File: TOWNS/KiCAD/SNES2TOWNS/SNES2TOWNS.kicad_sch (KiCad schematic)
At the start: 13 parts, among them J1 DE9_Receptacle, J2 ArduinoP2_P7, J3 ArduinoP8_P13, J4 ArduinoA5_A0, J5 ArduinoVCC_GND, J6 SNES_CONTROLLER, J7 Conn_02x03_Odd_Even, U1 74LS157, U2 74LS157

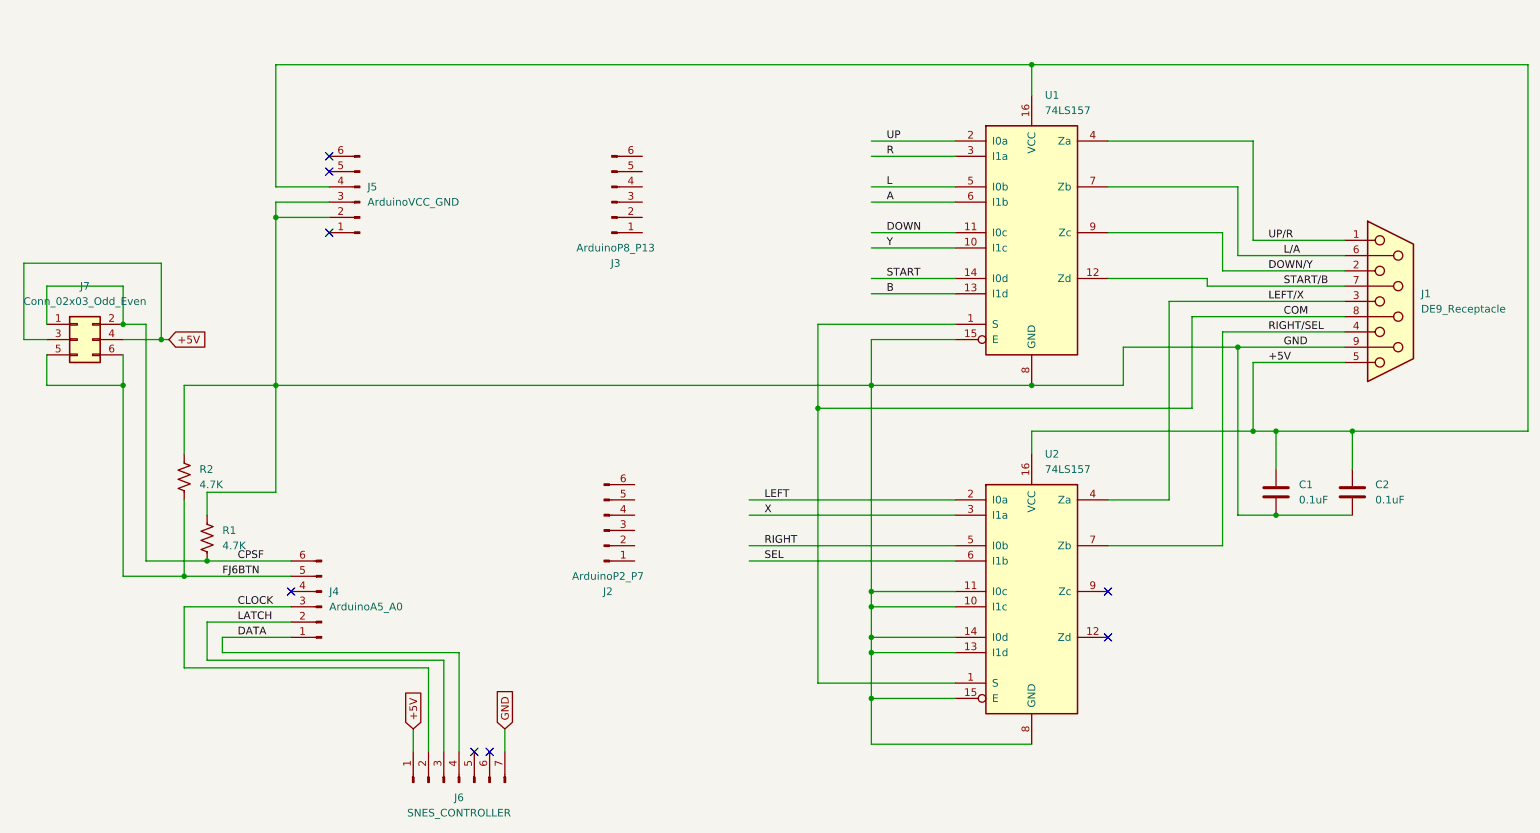
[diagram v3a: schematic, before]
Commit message: Change of plan.  PCB version will be for Arduino NANO.
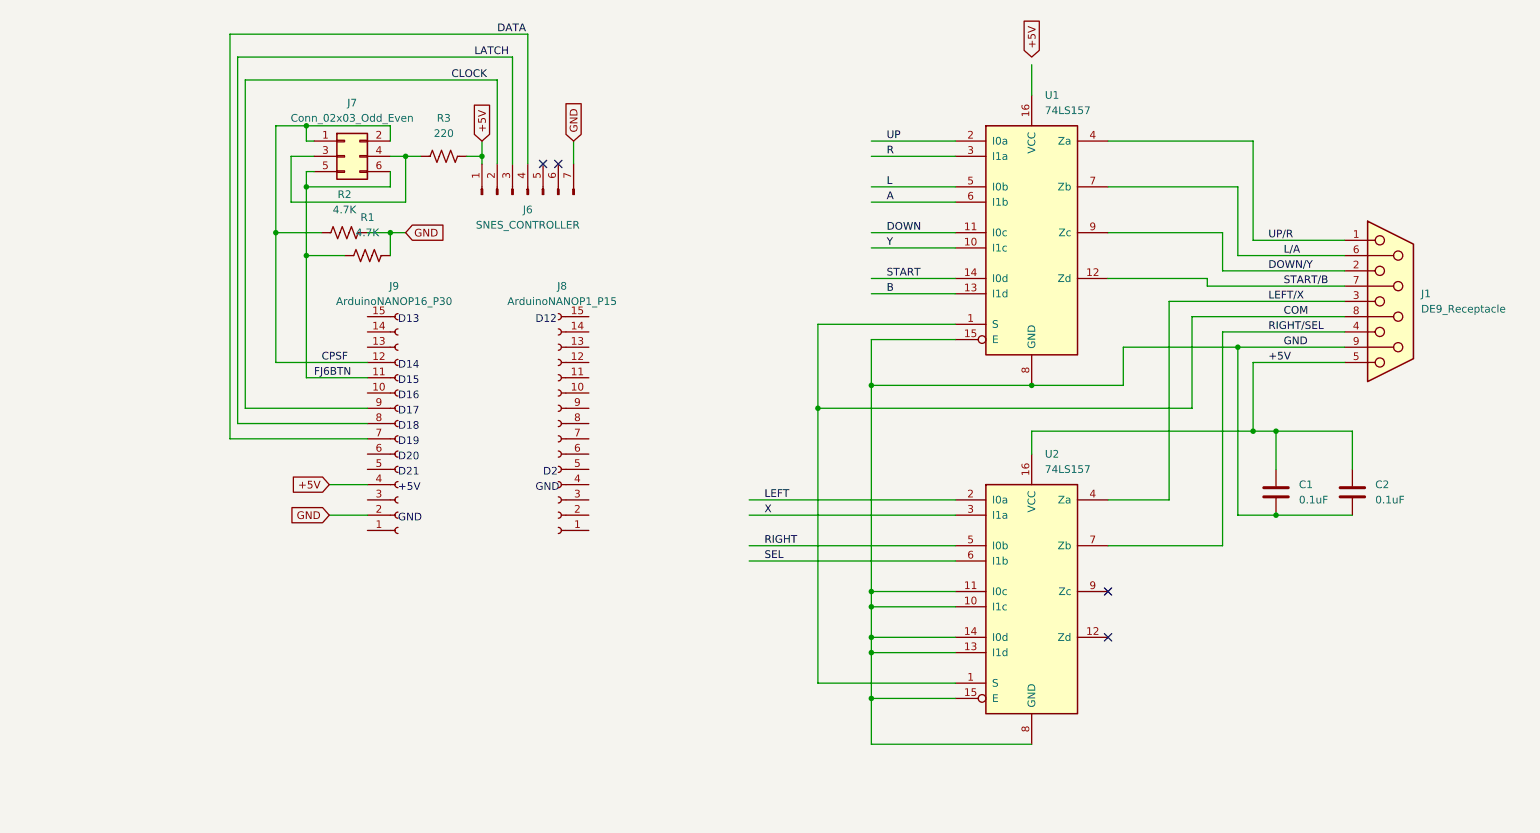
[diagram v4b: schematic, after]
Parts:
- removed J2: ArduinoP2_P7, Connector_PinHeader_2.54mm:PinHeader_1x06_P2.54mm_Vertical, symbol Connector:Conn_01x06_Pin
- removed J3: ArduinoP8_P13, Connector_PinHeader_2.54mm:PinHeader_1x06_P2.54mm_Vertical, symbol Connector:Conn_01x06_Pin
- removed J4: ArduinoA5_A0, Connector_PinHeader_2.54mm:PinHeader_1x06_P2.54mm_Vertical, symbol Connector:Conn_01x06_Pin
- removed J5: ArduinoVCC_GND, Connector_PinHeader_2.54mm:PinHeader_1x06_P2.54mm_Vertical, symbol Connector:Conn_01x06_Pin
- added J8: ArduinoNANOP1_P15, Connector_PinSocket_2.54mm:PinSocket_1x15_P2.54mm_Vertical, symbol Connector:Conn_01x15_Socket
- added J9: ArduinoNANOP16_P30, Connector_PinSocket_2.54mm:PinSocket_1x15_P2.54mm_Vertical, symbol Connector:Conn_01x15_Socket
- added R3: 220, Resistor_THT:R_Axial_DIN0207_L6.3mm_D2.5mm_P10.16mm_Horizontal, symbol Device:R_US
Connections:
- net +5V: now also J9.4 (Pin_4), R3.2; no longer J7.3 (Pin_3), J7.4 (Pin_4), U1.16 (VCC)
- net CLOCK: now also J9.9 (Pin_9)
- net CPSF: now also R2.1, J9.12 (Pin_12); no longer R1.2
- net DATA: now also J9.7 (Pin_7)
- net FJ6BTN: now also R1.1, J9.11 (Pin_11); no longer R2.2
- net GND: now also R1.2, R2.2, J9.2 (Pin_2); no longer R1.1, R2.1
- net LATCH: now also J9.8 (Pin_8)
- new net: J7.3 (Pin_3), J7.4 (Pin_4), R3.1
- no-connect marks 8 -> 4
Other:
- note added: "+5V"
- note added: "D12"
- note added: "D13"
- note added: "D14"
- note added: "D15"
- note added: "D16"
- note added: "D17"
- note added: "D18"
- note added: "D19"
- note added: "D2"
- note added: "D20"
- note added: "D21"
- note added: "GND"
- moved on the sheet: J6, J7, R1, R2

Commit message: Changed registers and capacitors from THT to SMD.
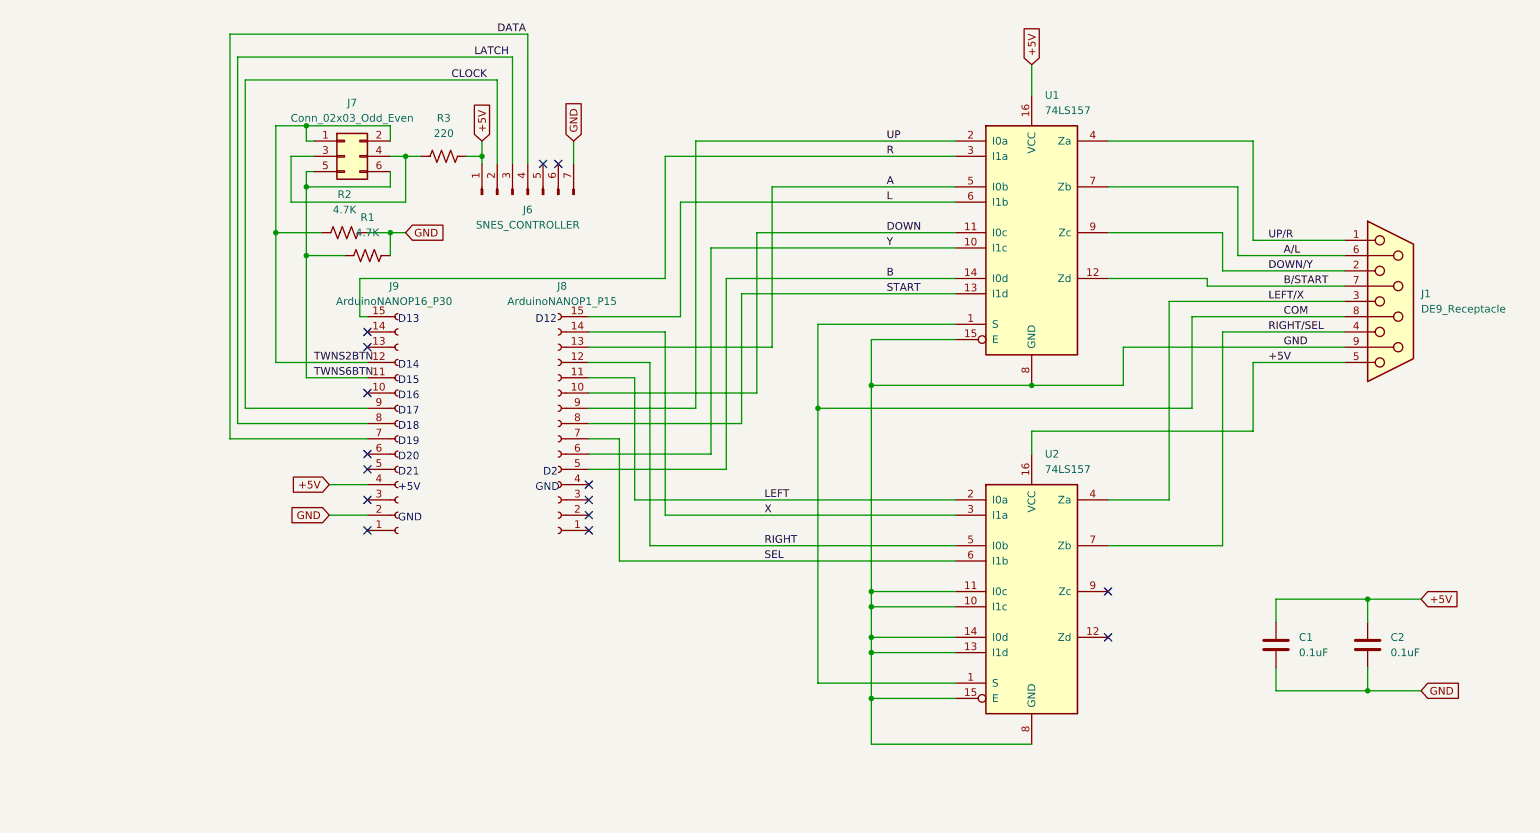
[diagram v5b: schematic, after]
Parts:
- C1, C2: footprint Capacitor_THT:C_Disc_D5.0mm_W2.5mm_P5.00mm -> Capacitor_SMD:C_0805_2012Metric_Pad1.18x1.45mm_HandSolder
- R1, R2, R3: footprint Resistor_THT:R_Axial_DIN0207_L6.3mm_D2.5mm_P10.16mm_Horizontal -> Resistor_SMD:R_0805_2012Metric_Pad1.20x1.40mm_HandSolder
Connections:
- net +5V: now also U1.16 (VCC)
- net A: now also J8.13 (Pin_13), U1.5 (I0b); no longer U1.6 (I1b)
- net B: now also J8.5 (Pin_5), U1.14 (I0d); no longer U1.13 (I1d)
- net DOWN: now also J8.10 (Pin_10)
- net L: now also J8.15 (Pin_15), U1.6 (I1b); no longer U1.5 (I0b)
- net LEFT: now also J8.11 (Pin_11)
- net R: now also J9.15 (Pin_15)
- net RIGHT: now also J8.12 (Pin_12)
- net SEL: now also J8.7 (Pin_7)
- net START: now also J8.8 (Pin_8), U1.13 (I1d); no longer U1.14 (I0d)
- net UP: now also J8.9 (Pin_9)
- net X: now also J8.14 (Pin_14)
- net Y: now also J8.6 (Pin_6)
- net CPSF renamed TWNS2BTN
- net FJ6BTN renamed TWNS6BTN
- net L/A renamed A/L
- net START/B renamed B/START
- no-connect marks 4 -> 15
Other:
- moved on the sheet: C1, C2

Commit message: Design Change
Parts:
- J7: value Conn_02x03_Odd_Even -> Slide Switch
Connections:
- net A renamed OUT_P2A
- net OUT_P2A: now also J8.14 (Pin_14); no longer J8.13 (Pin_13)
- net A/L renamed OUT_P2
- net OUT_P2: now also J1.2; no longer J1.6
- net B renamed OUT_P4A
- net OUT_P4A: now also J8.10 (Pin_10); no longer J8.5 (Pin_5)
- net B/START renamed OUT_P4
- net OUT_P4: now also J1.4; no longer J1.7
- net DOWN renamed OUT_P3A
- net OUT_P3A: now also J8.12 (Pin_12); no longer J8.10 (Pin_10)
- net DOWN/Y renamed OUT_P3
- net OUT_P3: now also J1.3; no longer J1.2
- net L renamed OUT_P1B
- net OUT_P1B: now also U1.3 (I1a); no longer U1.6 (I1b)
- net LEFT renamed OUT_P3B
- net OUT_P3B: now also U1.10 (I1c); no longer U2.2 (I0a)
- net LEFT/X renamed OUT_P6
- net OUT_P6: now also J1.6; no longer J1.3
- net R renamed OUT_P1A
- net OUT_P1A: now also U1.2 (I0a); no longer U1.3 (I1a)
- net RIGHT renamed OUT_P7A
- net OUT_P7A: now also J8.6 (Pin_6); no longer J8.12 (Pin_12)
- net RIGHT/SEL renamed OUT_P7
- net OUT_P7: now also J1.7; no longer J1.4
- net SEL renamed OUT_P6B
- net OUT_P6B: now also U2.3 (I1a); no longer U2.6 (I1b)
- net START renamed OUT_P4B
- net OUT_P4B: now also J8.9 (Pin_9); no longer J8.8 (Pin_8)
- removed net UP: J8.9 (Pin_9), U1.2 (I0a)
- net UP/R renamed OUT_P1
- removed net X: J8.14 (Pin_14), U2.3 (I1a)
- removed net Y: J8.6 (Pin_6), U1.10 (I1c)
- new net OUT_P2B: J8.13 (Pin_13), U1.6 (I1b)
- new net OUT_P6A: J8.8 (Pin_8), U2.2 (I0a)
- new net OUT_P7B: J8.5 (Pin_5), U2.6 (I1b)
